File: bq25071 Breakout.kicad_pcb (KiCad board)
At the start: 2 copper layers, 25 x 25 mm, 21 parts, among them P1 USB_OTG, P2 CONN_01X05, P3 CONN_01X04, P4 CONN_01X02, U1 bq25071

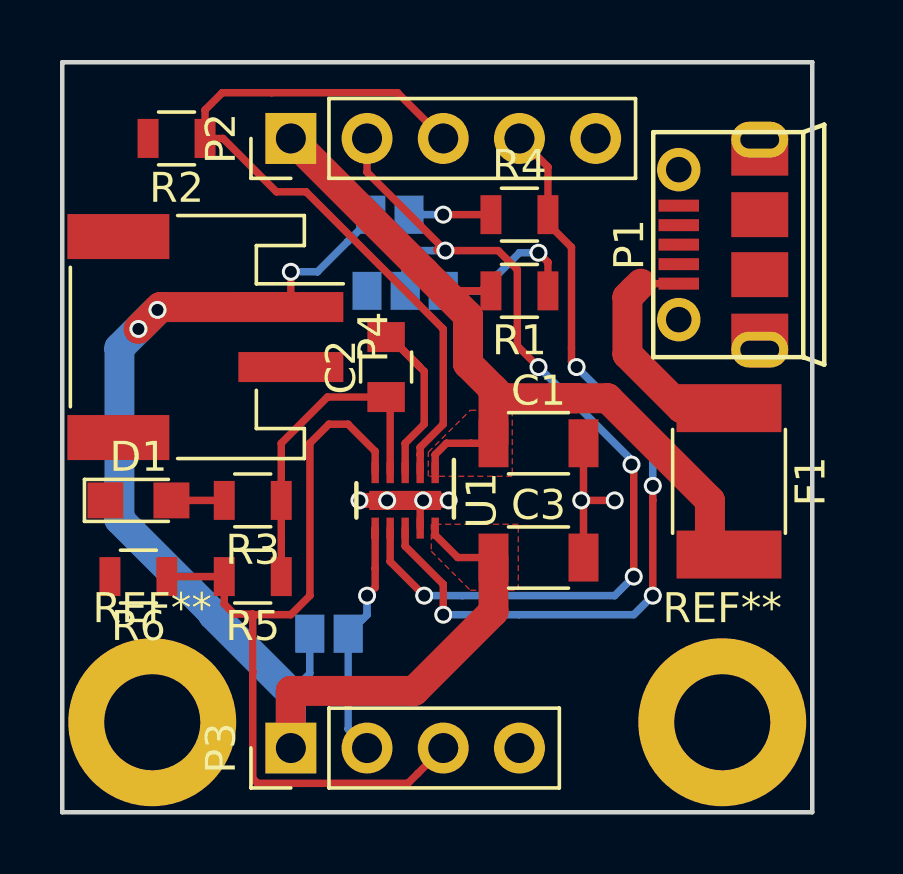
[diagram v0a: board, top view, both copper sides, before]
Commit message: better component placement
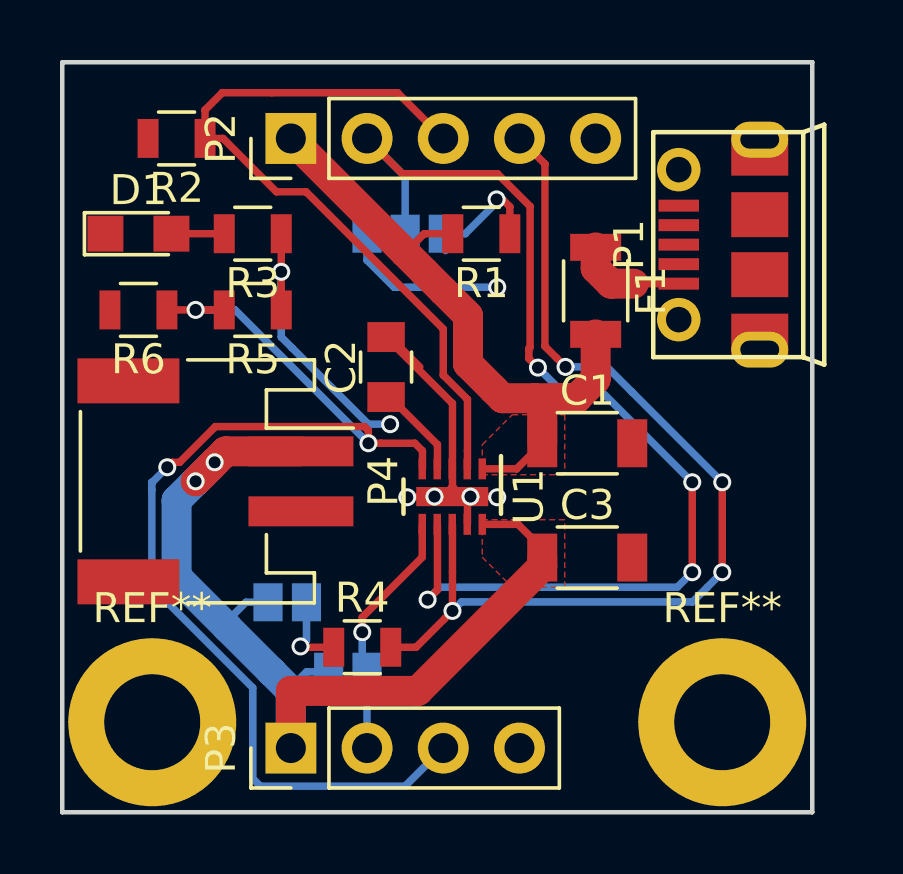
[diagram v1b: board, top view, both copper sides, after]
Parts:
- F1: footprint Resistors_SMD:R_1812 -> Resistors_SMD:R_1206
- moved R4 15.3 mm to (100.0, 129.5)
- moved GS3 13.4 mm to (97.5, 128.0)
- moved D1 8.89 mm to (92.5, 115.7)
- moved R3 8.89 mm to (96.3, 115.7)
- moved R5 8.89 mm to (96.3, 118.3)
- moved R6 8.89 mm to (92.5, 118.3)
- moved F1 7.75 mm to (107.8, 117.6)
- moved P4 4.82 mm to (95.1, 124.0)
- moved R1 2.29 mm to (104.0, 115.7)
- moved GS1 1.91 mm to (101.4, 115.7)
- moved C1 1.62 mm to (107.5, 122.7)
- moved C3 1.62 mm to (107.5, 126.5)
- moved U1 1.58 mm to (103.0, 124.5)
- moved GS2 1.42 mm to (99.5, 130.3)
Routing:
- net /TS: track 27.1 -> 38.7 mm, vias 0 -> 3
- net +BATT: track 44.1 -> 37.8 mm, vias 3 -> 2
- net VCC: track 28.6 -> 23.1 mm
- net /CHG: track 27.7 -> 33.0 mm
- net /EN: track 32.4 -> 37.2 mm, vias 5 -> 4
- net Net-(F1-Pad1): track 7.29 -> 3.68 mm
- net GND: track 14.7 -> 17.5 mm, vias 6 -> 5
- net /LDO: track 11.2 -> 13.2 mm, vias 0 -> 2
- net Net-(GS1-Pad1): track 5.10 -> 3.80 mm

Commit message: silkscreen
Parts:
- added REF***: OSHW-Logo2_7.3x6mm_SilkScreen, Symbols:OSHW-Logo2_7.3x6mm_SilkScreen, B.Cu at (107.5, 123.5)
-  : renamed from GS1
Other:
- board text added: "+BAT"
- board text added: "-EN+"
- board text added: "BAT SENS"
- board text added: "CHG"
- board text added: "CHG Pullup"
- board text added: "EN"
- board text added: "GND"
- board text added: "Iset"
- board text added: "S"
- board text added: "SENS"
- board text added: "TEMP"
- board text added: "VCC"
- board text added: "bq25071 LiFePo4 Charger 1A"
- board text added: "by Florian Winkler"

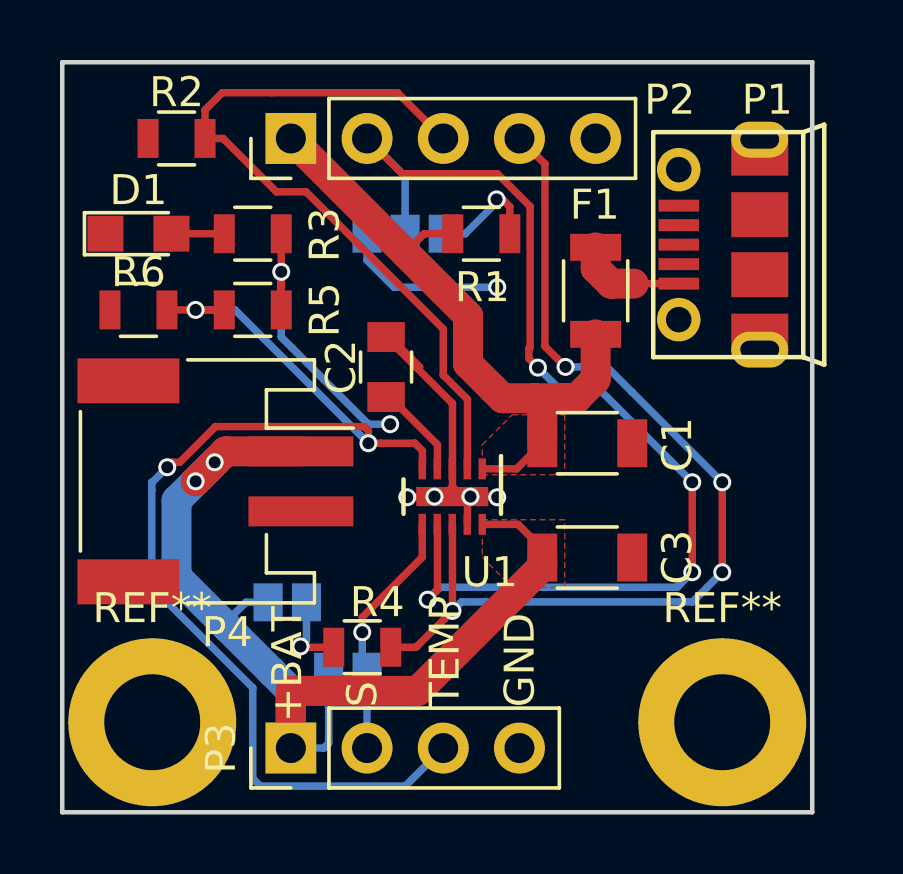
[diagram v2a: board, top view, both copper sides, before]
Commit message: change battery connector to jst xh (seems to be standard for rc lipos)
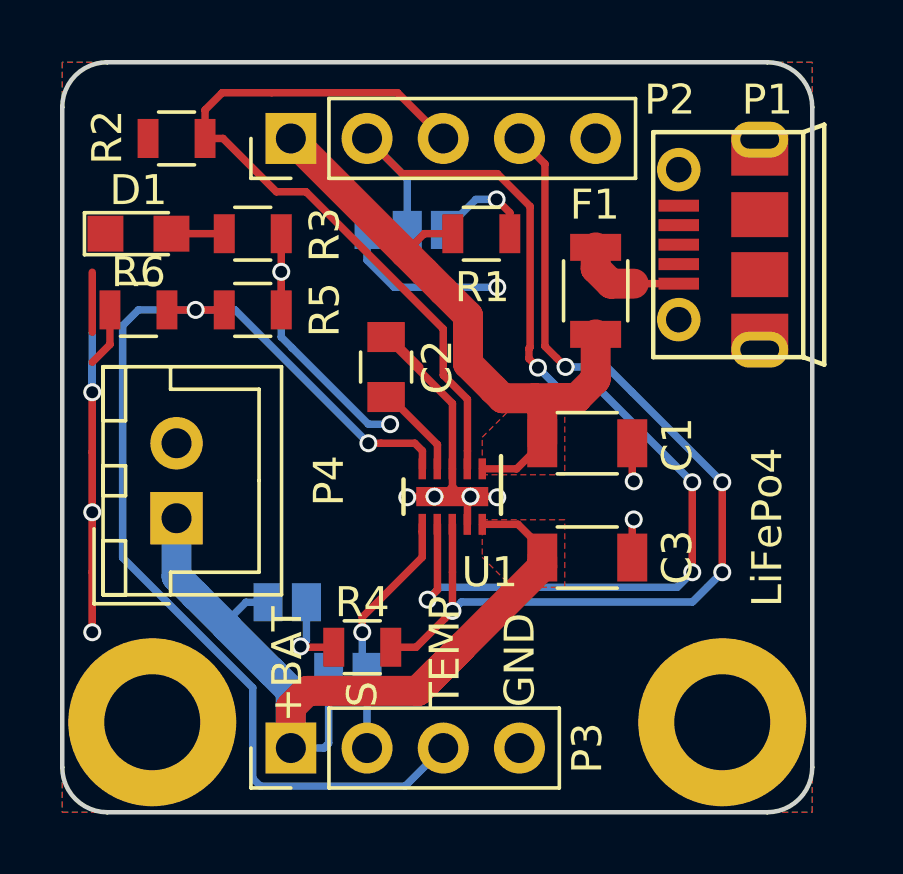
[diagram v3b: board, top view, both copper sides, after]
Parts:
- removed  : GS3, Connect:GS3
- added GS1: GS3, Connect:GS3, B.Cu at (101.5, 115.6)
- P4: footprint Connectors_JST:JST_PH_S2B-PH-SM4-TB_02x2.00mm_Angled -> Connectors_JST:JST_XH_B02B-XH-A_02x2.50mm_Straight
- moved P4 1.77 mm to (93.8, 125.2), turned to 90 degrees
- turned REF*** to 0 degrees
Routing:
- net GND: track 17.5 -> 43.1 mm, vias 5 -> 10
- net +BATT: track 38.0 -> 34.1 mm, vias 2 -> 0
- net /TS: track 38.7 -> 38.5 mm, vias 3 -> 2
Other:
- outline, holes or cut-outs redrawn
- board text added: "LiFePo4"
- board text added: "bq25071 LiFePo4 1A Charger"
- board text removed: "bq25071 LiFePo4 Charger 1A"

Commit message: silkscreen
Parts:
- moved REF*** 14.4 mm to (93.8, 118.9), turned to 90 degrees
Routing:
- net GND: track 43.1 -> 22.1 mm, vias 10 -> 7
- net (no net): track 0.00 -> 21.0 mm, vias 0 -> 3
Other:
- board text added: "bq25071 LiFePo4 1A Charger v1 by @kugel2"
- board text removed: "bq25071 LiFePo4 1A Charger"
- board text removed: "by Florian Winkler"
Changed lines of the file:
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@@
 (kicad_pcb (version 4) (host pcbnew 4.0.5)
   (general
-    (links 50)
-    (no_connects 4)
+    (links 47)
+    (no_connects 1)
     (area 89.924999 109.924999 115.075001 135.075001)
     (thickness 1.6)
-    (drawings 30)
+    (drawings 29)
     (tracks 202)
     (zones 0)
@@
   )
   (module Symbols:OSHW-Logo2_7.3x6mm_SilkScreen (layer B.Cu)
-    (at 107.5 123.5)
+    (at 93.81 118.89 90)
     (descr "Open Source Hardware Symbol")
     (tags "Logo Symbol OSHW")
     (attr virtual)
-    (fp_text reference REF*** (at 0 0) (layer B.SilkS) hide
+    (fp_text reference REF*** (at 0 0 90) (layer B.SilkS) hide
       (effects (font (size 1 1) (thickness 0.15)) (justify mirror))
     )
-    (fp_text value OSHW-Logo2_7.3x6mm_SilkScreen (at 0.75 0) (layer B.Fab) hide
+    (fp_text value OSHW-Logo2_7.3x6mm_SilkScreen (at 0.75 0 90) (layer B.Fab) hide
       (effects (font (size 1 1) (thickness 0.15)) (justify mirror))
     )
@@
     (tags "solder bridge")
     (attr smd)
-    (fp_text reference GS1 (at -1.7 0 360) (layer B.SilkS)
+    (fp_text reference GS1 (at -1.7 0 180) (layer B.SilkS) hide
       (effects (font (size 1 1) (thickness 0.15)) (justify mirror))
     )
@@
     (descr "JST XH series connector, B02B-XH-A, top entry type, through hole")
     (tags "connector jst xh tht top vertical 2.50mm")
-    (fp_text reference P4 (at 1.25 5.08 270) (layer F.SilkS)
+    (fp_text reference P4 (at -3.215 1.27 360) (layer F.SilkS)
       (effects (font (size 1 1) (thickness 0.15)))
     )
@@
     )
   )
-  (gr_text LiFePo4 (at 113.5 125.5 90) (layer F.SilkS)
+  (gr_text LiFePo4 (at 98.255 123.97 90) (layer F.SilkS)
     (effects (font (size 1 1) (thickness 0.2)))
   )
@@
     (effects (font (size 1 1) (thickness 0.2)) (justify mirror))
   )
-  (gr_text "bq25071\nLiFePo4\n1A Charger" (at 93 111 90) (layer B.SilkS)
+  (gr_text "bq25071\nLiFePo4\n1A Charger\nv1 by @kugel2" (at 109.05 120.795 360) (layer B.SilkS)
     (effects (font (size 1 1) (thickness 0.1)) (justify left mirror))
   )
@@
   (gr_text GND (at 105.25 131.5 90) (layer F.SilkS)
     (effects (font (size 1 1) (thickness 0.2)) (justify left))
-  )
-  (gr_text "by\nFlorian\nWinkler" (at 96.985 121.43 90) (layer B.SilkS)
-    (effects (font (size 1 1) (thickness 0.1)) (justify mirror))
   )
   (gr_line (start 113.5 135) (end 91.5 135) (layer Edge.Cuts) (width 0.15))
@@
   (gr_line (start 91.5 110) (end 113.5 110) (layer Edge.Cuts) (width 0.15))
   (gr_line (start 90 133.5) (end 90 111.5) (layer Edge.Cuts) (width 0.15))
+  (segment (start 91 119) (end 91 117) (width 0.25) (layer F.Cu) (net 0))
+  (segment (start 91 121) (end 91 119) (width 0.25) (layer B.Cu) (net 0))
+  (segment (start 91 123) (end 91 121) (width 0.25) (layer F.Cu) (net 0))
+  (via (at 91 121) (size 0.6) (drill 0.4) (layers F.Cu B.Cu) (net 0))
+  (segment (start 91 125) (end 91 123) (width 0.25) (layer F.Cu) (net 0))
+  (segment (start 91 127) (end 91 125) (width 0.25) (layer F.Cu) (net 0))
+  (via (at 91 125) (size 0.6) (drill 0.4) (layers F.Cu B.Cu) (net 0))
+  (segment (start 91 129) (end 91 127) (width 0.25) (layer F.Cu) (net 0))
+  (segment (start 91 120) (end 91 129) (width 0.25) (layer B.Cu) (net 0))
+  (via (at 91 129) (size 0.6) (drill 0.4) (layers F.Cu B.Cu) (net 0))
   (segment (start 104.674999 121.199999) (end 105.75 121.199999) (width 1) (layer F.Cu) (net 1))
   (segment (start 105.75 121.199999) (end 107.145 121.199999) (width 1) (layer F.Cu) (net 1))
@@
   (segment (start 109 123.92) (end 109.05 123.97) (width 0.25) (layer F.Cu) (net 2))
   (via (at 109.05 123.97) (size 0.6) (drill 0.4) (layers F.Cu B.Cu) (net 2))
-  (segment (start 91 119) (end 91 117) (width 0.25) (layer F.Cu) (net 2))
-  (segment (start 91 121) (end 91 119) (width 0.25) (layer B.Cu) (net 2))
-  (segment (start 91 123) (end 91 121) (width 0.25) (layer F.Cu) (net 2))
-  (via (at 91 121) (size 0.6) (drill 0.4) (layers F.Cu B.Cu) (net 2))
-  (segment (start 91 125) (end 91 123) (width 0.25) (layer F.Cu) (net 2))
-  (segment (start 91 127) (end 91 125) (width 0.25) (layer F.Cu) (net 2))
-  (via (at 91 125) (size 0.6) (drill 0.4) (layers F.Cu B.Cu) (net 2))
-  (segment (start 91 129) (end 91 127) (width 0.25) (layer F.Cu) (net 2))
-  (segment (start 91 120) (end 91 129) (width 0.25) (layer B.Cu) (net 2))
-  (via (at 91 129) (size 0.6) (drill 0.4) (layers F.Cu B.Cu) (net 2))
   (segment (start 91.59 118.255) (end 91.59 119.41) (width 0.25) (layer F.Cu) (net 2))
   (segment (start 91.59 119.41) (end 91 120) (width 0.25) (layer F.Cu) (net 2))
